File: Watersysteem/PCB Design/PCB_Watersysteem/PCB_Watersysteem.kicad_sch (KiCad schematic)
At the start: 36 parts, among them J1 Screw_Terminal_01x02, J2 Conn_01x04_Pin, K1 AHQSS105DM2FA0G, K2 AHQSS105DM2FA0G, K3 AHQSS105DM2FA0G, K4 AHQSS105DM2FA0G, SW1 EN, SW2 BOOT, U1 ESP32-WROOM-32D, U2 MP1584_Module, U3 AMS1117-3.3, U4 ADS1115IDGS

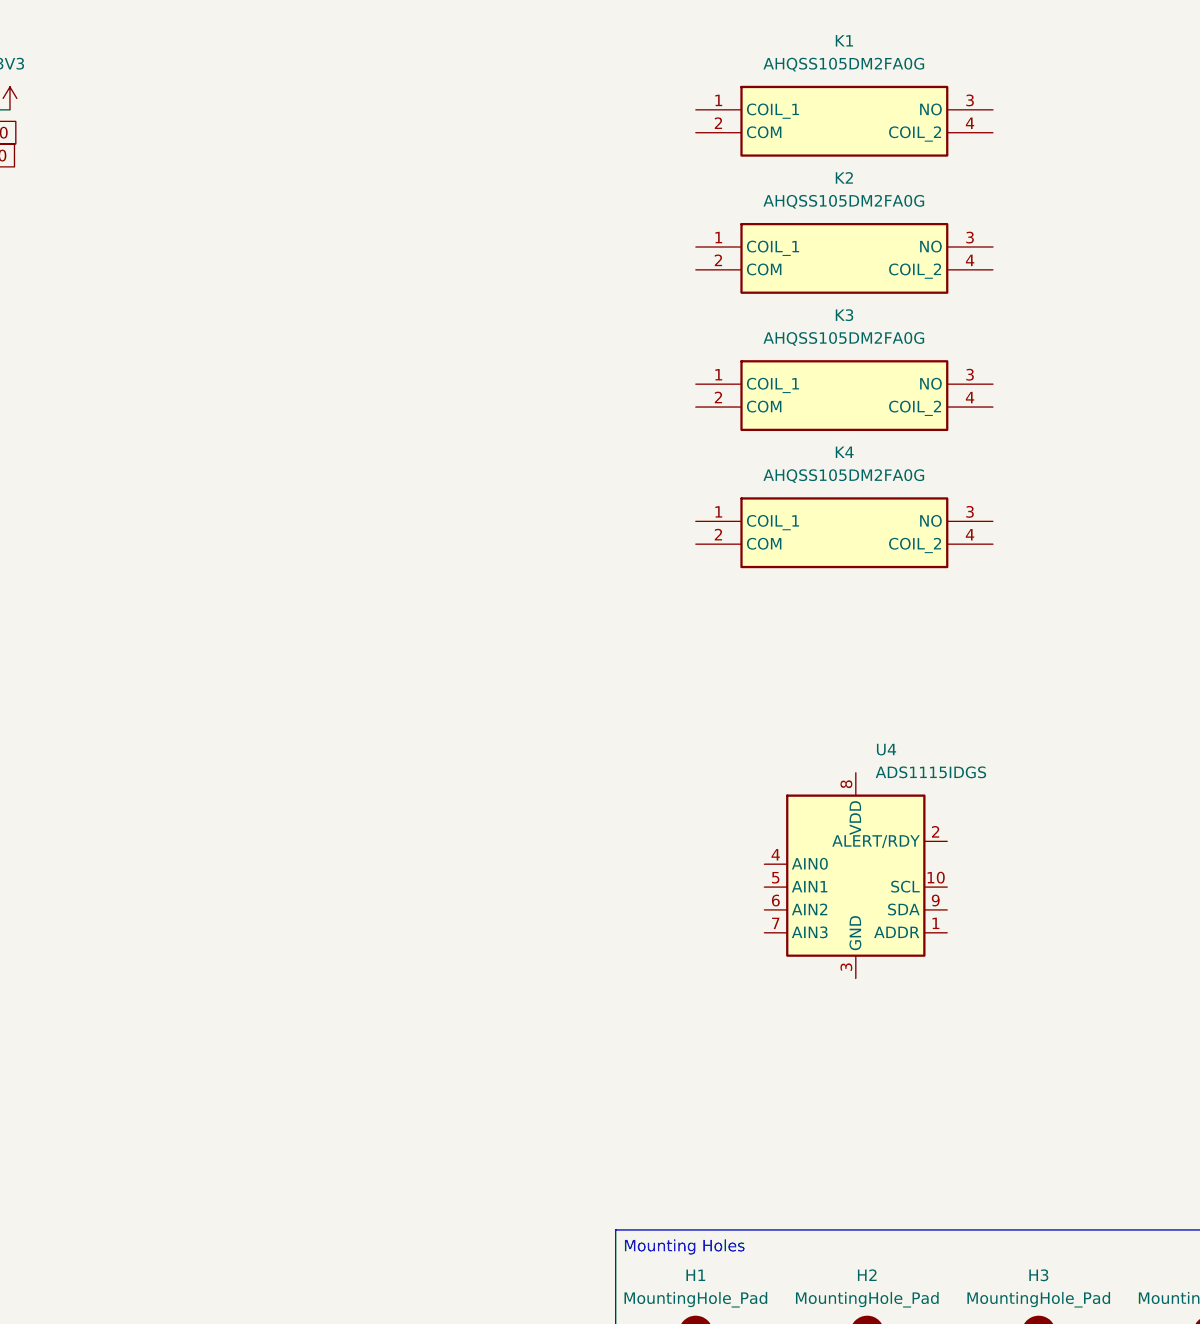
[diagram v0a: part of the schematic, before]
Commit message: Update PCB watersysteem
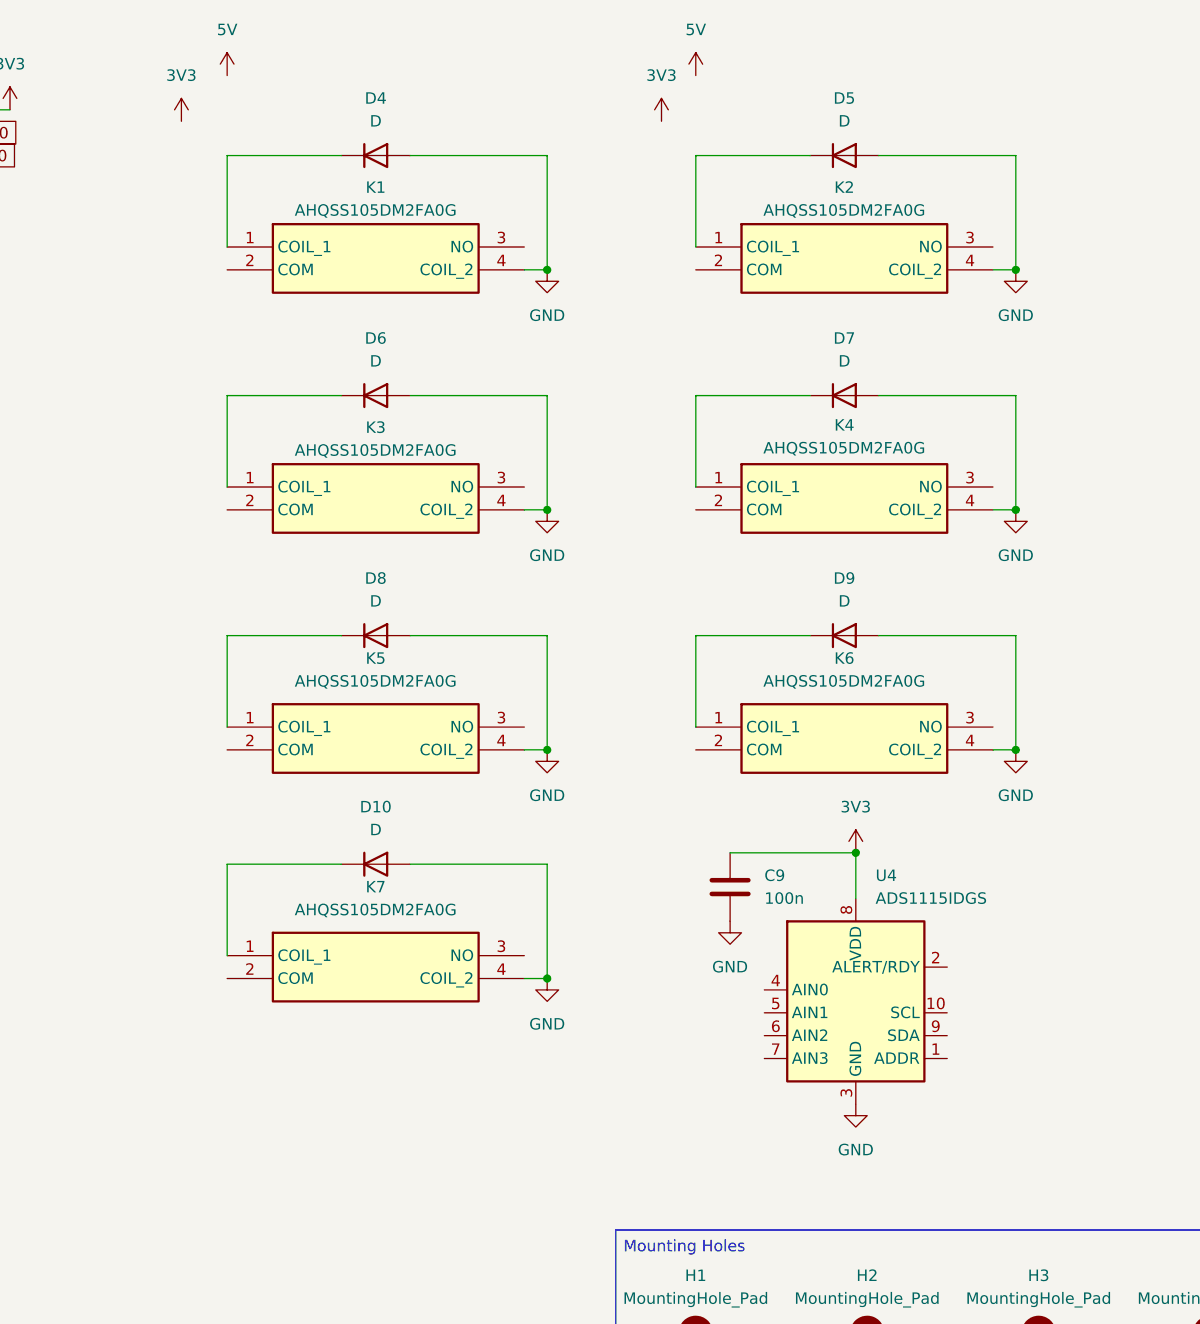
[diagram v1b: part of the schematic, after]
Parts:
- added C9: 100n, symbol Device:C
- added D10, D4, D5, D6, D7, D8, D9: D, symbol Device:D
- added K5, K6, K7: AHQSS105DM2FA0G, AHQSS105DM2FA0G, symbol SamacSys_Parts:AHQSS105DM2FA0G
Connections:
- net 3V3: now also U4.8 (VDD), C9.1
- net GND: now also K1.4 (COIL_2), K2.4 (COIL_2), K3.4 (COIL_2), K4.4 (COIL_2), U4.3 (GND), C9.2, D10.2 (A), D4.2 (A), D5.2 (A), D6.2 (A), D7.2 (A), D8.2 (A), D9.2 (A), K5.4 (COIL_2), K6.4 (COIL_2), K7.4 (COIL_2)
- net at K1.1 (COIL_1): now also D4.1 (K)
- net at K3.1 (COIL_1): now also D6.1 (K)
- net at K2.1 (COIL_1): now also D5.1 (K)
- net at K4.1 (COIL_1): now also D7.1 (K)
- new net: D9.1 (K), K6.1 (COIL_1)
- new net: D10.1 (K), K7.1 (COIL_1)
- new net: D8.1 (K), K5.1 (COIL_1)
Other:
- moved on the sheet: K1, K3, K4, U4

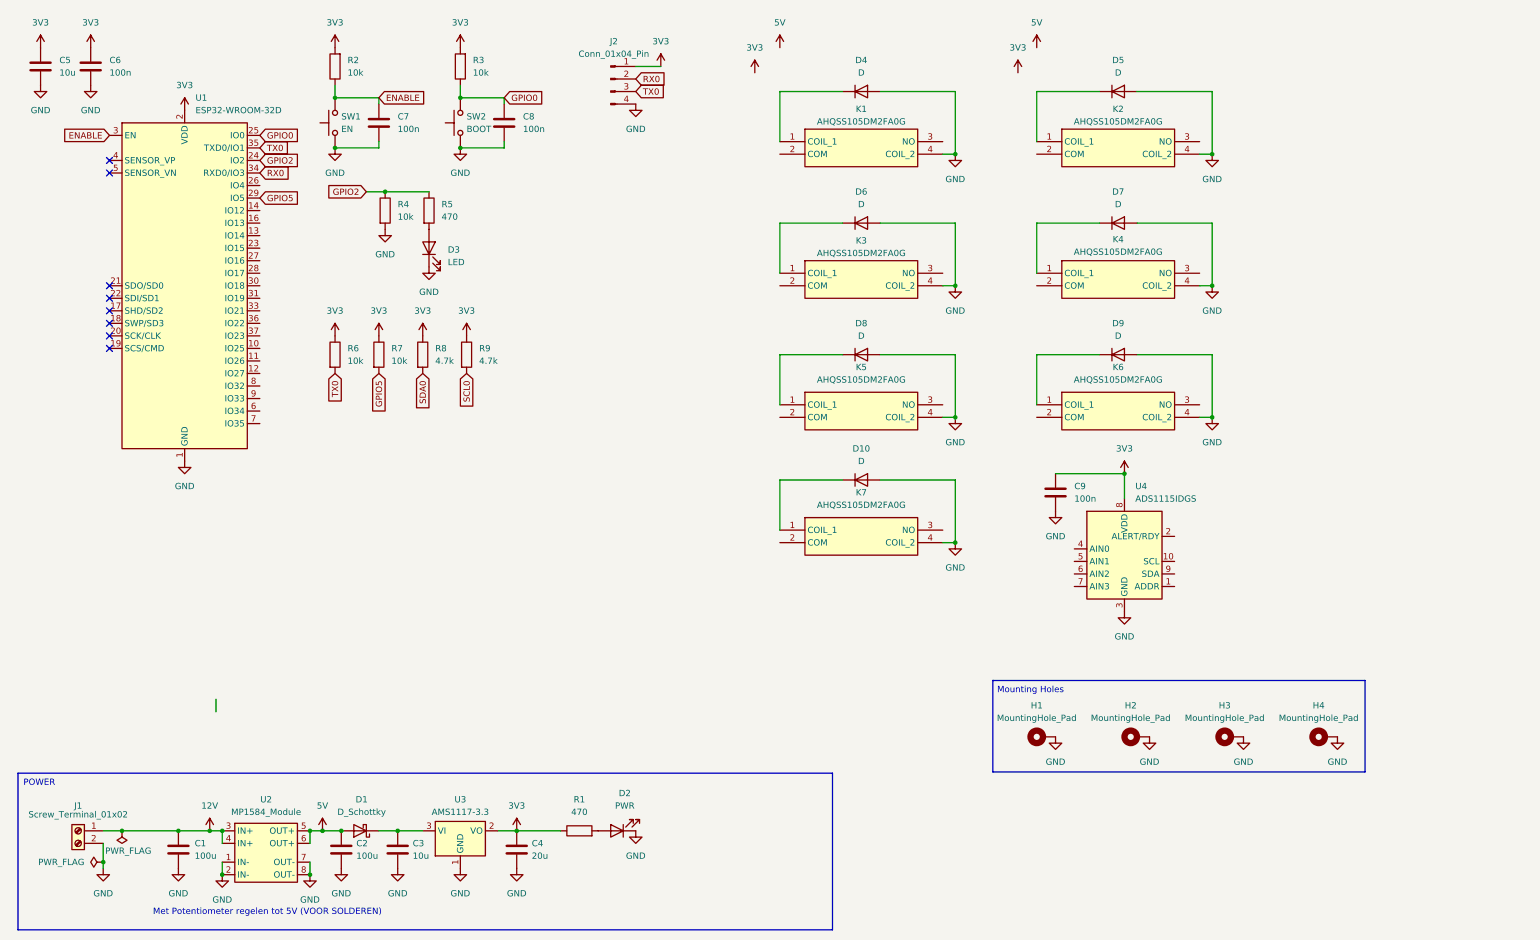
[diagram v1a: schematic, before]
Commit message: PCB update
ADC verbonden, LED outputs, Eindeloops, Voorbeeld relais
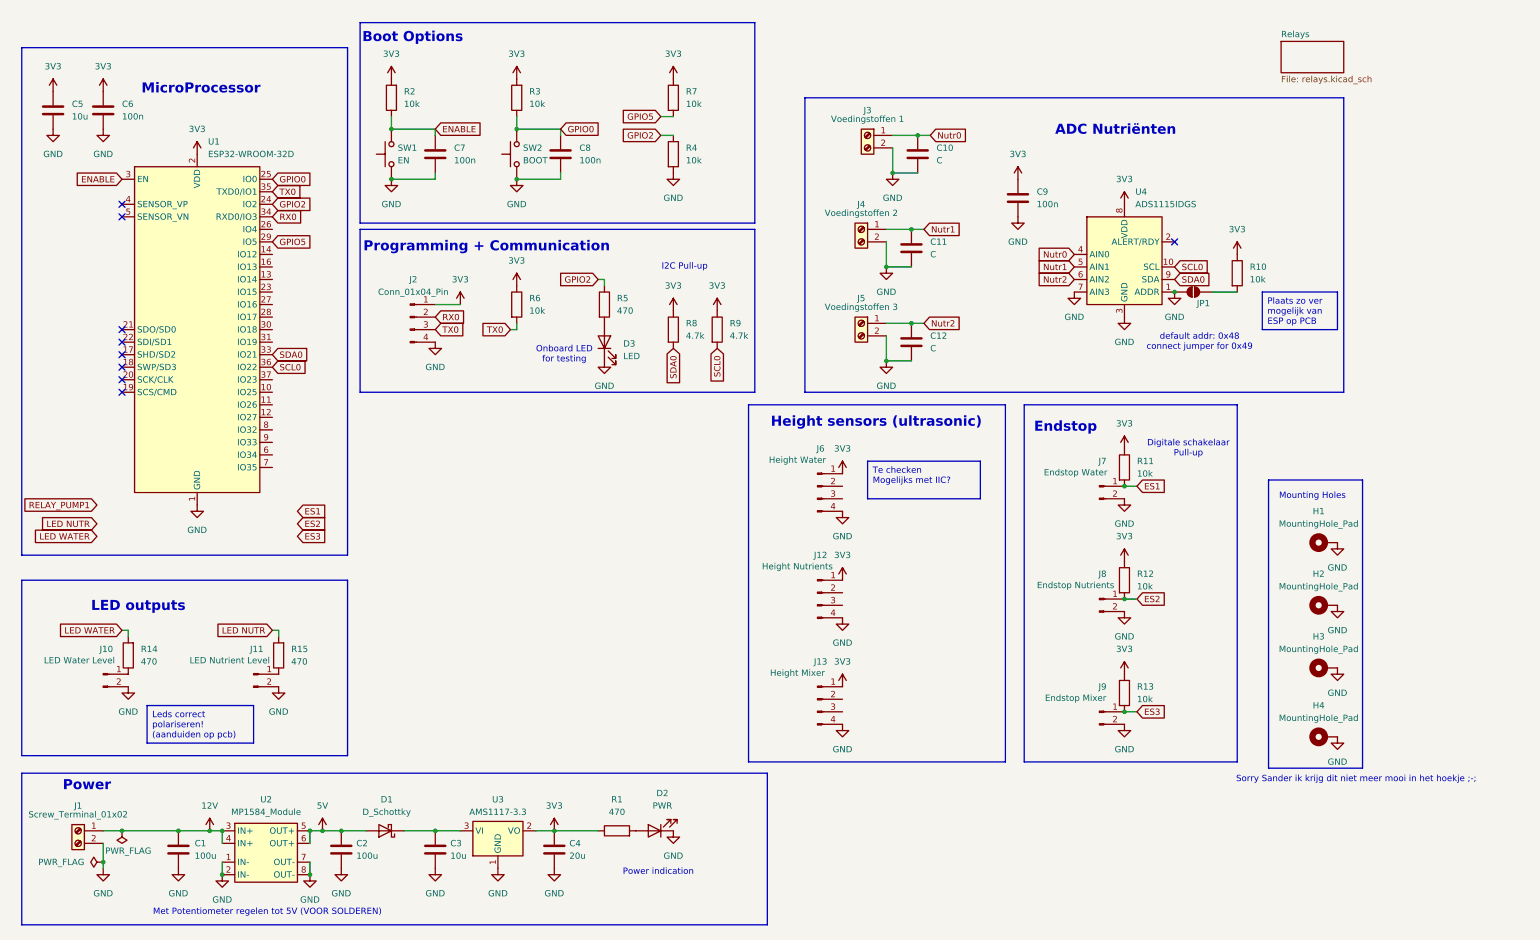
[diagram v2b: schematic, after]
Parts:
- removed D10, D4, D5, D6, D7, D8, D9: D, symbol Device:D
- removed K1, K2, K3, K4, K5, K6, K7: AHQSS105DM2FA0G, AHQSS105DM2FA0G, symbol SamacSys_Parts:AHQSS105DM2FA0G
- added C10, C11, C12: C, symbol Device:C
- added J10: LED Water Level, symbol Connector:Conn_01x02_Pin
- added J11: LED Nutrient Level, symbol Connector:Conn_01x02_Pin
- added J12: Height Nutrients, symbol Connector:Conn_01x04_Pin
- added J13: Height Mixer, symbol Connector:Conn_01x04_Pin
- added J3: Voedingstoffen 1, symbol Connector:Screw_Terminal_01x02
- added J4: Voedingstoffen 2, symbol Connector:Screw_Terminal_01x02
- added J5: Voedingstoffen 3, symbol Connector:Screw_Terminal_01x02
- added J6: Height Water, symbol Connector:Conn_01x04_Pin
- added J7: Endstop Water, symbol Connector:Conn_01x02_Pin
- added J8: Endstop Nutrients, symbol Connector:Conn_01x02_Pin
- added J9: Endstop Mixer, symbol Connector:Conn_01x02_Pin
- added JP1: SolderJumper_2_Open, symbol Jumper:SolderJumper_2_Open
- added R10, R11, R12, R13: 10k, symbol Device:R
- added R14, R15: 470, symbol Device:R
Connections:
- net 3V3: now also J12.1 (Pin_1), J13.1 (Pin_1), J6.1 (Pin_1), R10.1, R11.1, R12.1, R13.1
- net GND: now also U4.1 (ADDR), U4.7 (AIN3), C10.2, C11.2, C12.2, J10.2 (Pin_2), J11.2 (Pin_2), J12.4 (Pin_4), J13.4 (Pin_4), J3.2 (Pin_2), J4.2 (Pin_2), J5.2 (Pin_2), J6.4 (Pin_4), J7.2 (Pin_2), J8.2 (Pin_2), J9.2 (Pin_2), JP1.1 (A)
- net SCL0: now also U1.36 (IO22), U4.10 (SCL)
- net SDA0: now also U1.33 (IO21), U4.9 (SDA)
- net Nutr0: now reaches U4.4 (AIN0)
- net Nutr0: now also C10.1, J3.1 (Pin_1)
- net Nutr1: now reaches U4.5 (AIN1)
- net Nutr1: now also C11.1, J4.1 (Pin_1)
- net Nutr2: now reaches U4.6 (AIN2)
- net Nutr2: now also C12.1, J5.1 (Pin_1)
- new net: J11.1 (Pin_1), R15.1
- new net: J10.1 (Pin_1), R14.1
- new net: JP1.2 (B), R10.2
- new net ES1: J7.1 (Pin_1), R11.2
- new net ES2: J8.1 (Pin_1), R12.2
- new net ES3: J9.1 (Pin_1), R13.2
- new net LED NUTR: R15.2
- new net LED WATER: R14.2
- no-connect marks 8 -> 9
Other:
- added sheet Relays (relays.kicad_sch)
- note added: "ADC Nutriënten"
- note added: "Boot Options"
- note added: "Digitale schakelaar Pull-up"
- note added: "Endstop"
- note added: "Height sensors (ultrasonic)"
- note added: "I2C Pull-up"
- note added: "LED outputs"
- note added: "MicroProcessor"
- note added: "Onboard LED for testing"
- note added: "Power"
- note added: "Power indication"
- note added: "Programming + Communication"
- note added: "Sorry Sander ik krijg dit niet meer mooi in het hoekje ;-;"
- note added: "default addr: 0x48 connect jumper for 0x49"
- note removed: "POWER"
- company: (none) -> KU Leuven
- title: (none) -> PCB Watersysteem
- moved on the sheet: C3, C4, C5, C6, C7, C8, C9, D1, D2, D3, H1, H2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

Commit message: Update PCB
Extra terminals
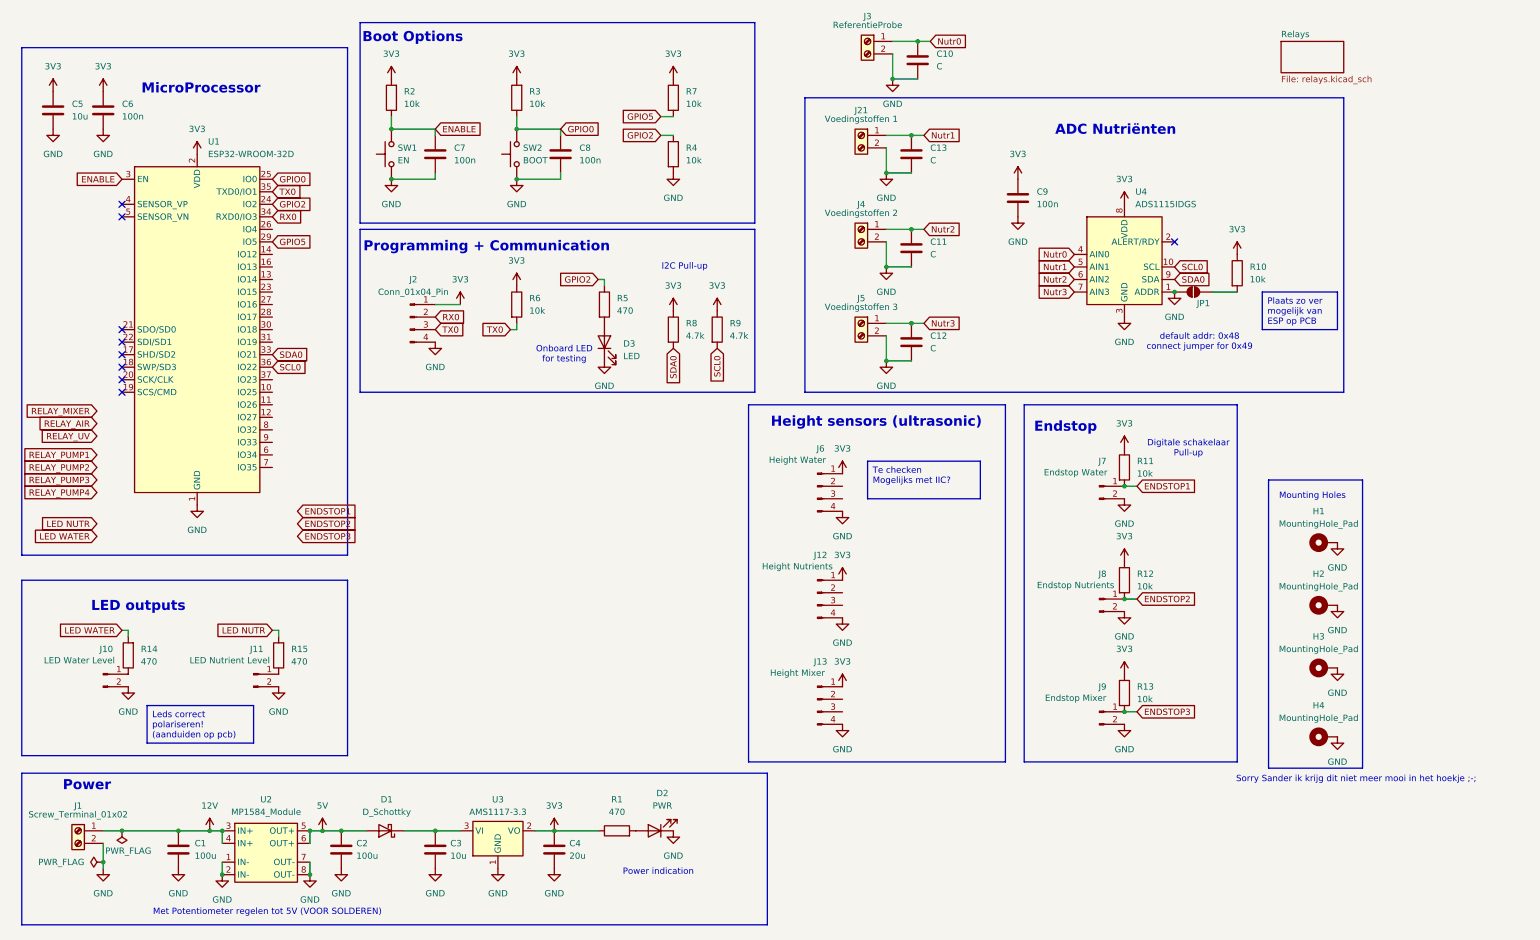
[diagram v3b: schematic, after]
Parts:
- added C13: C, symbol Device:C
- added J21: Voedingstoffen 1, symbol Connector:Screw_Terminal_01x02
- J3: value Voedingstoffen 1 -> ReferentieProbe
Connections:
- net GND: now also C13.2, J21.2 (Pin_2); no longer U4.7 (AIN3)
- net Nutr1: now also C13.1, J21.1 (Pin_1); no longer C11.1, J4.1 (Pin_1)
- net Nutr2: now also C11.1, J4.1 (Pin_1); no longer C12.1, J5.1 (Pin_1)
- net ES1 renamed ENDSTOP1
- net ES2 renamed ENDSTOP2
- net ES3 renamed ENDSTOP3
- new net Nutr3: C12.1, J5.1 (Pin_1), U4.7 (AIN3)
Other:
- moved on the sheet: C10, J3
